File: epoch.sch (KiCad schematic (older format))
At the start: 33 parts, among them J1 USB_OTG, J2 CONN_01X05, P3 CONN_01X10, SW1 SW_Reset, SW2 SW_Up, SW3 SW_Middle, SW4 SW_Down, U1 MIC5219-3.3BM5, U2 ATSAMD21Ennc-AU, U3 DS3231MZ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

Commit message: Increase drill size to 2.1.  Rework daughter board
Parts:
- U6, U7, U8, U9: footprint my-fp-library:MH2mm -> my-fp-library:MH2.1mm; symbol MH2mm -> MH2.1mm
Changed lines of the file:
@@
 $EndComp
 $Comp
-L MH2mm U6
+L MH2.1mm U6
 U 1 1 59C46AF5
 P 10350 2400
 F 0 "U6" H 10450 2400 60  0001 C CNN
 F 1 "MH2mm" H 10350 2700 60  0001 C CNN
-F 2 "my-fp-library:MH2mm" H 10350 2400 60  0001 C CNN
+F 2 "my-fp-library:MH2.1mm" H 10350 2400 60  0001 C CNN
 F 3 "" H 10350 2400 60  0001 C CNN
 	1    10350 2400
@@
 $EndComp
 $Comp
-L MH2mm U7
+L MH2.1mm U7
 U 1 1 59C46D36
 P 10350 2550
 F 0 "U7" H 10450 2550 60  0001 C CNN
 F 1 "MH2mm" H 10350 2850 60  0001 C CNN
-F 2 "my-fp-library:MH2mm" H 10350 2550 60  0001 C CNN
+F 2 "my-fp-library:MH2.1mm" H 10350 2550 60  0001 C CNN
 F 3 "" H 10350 2550 60  0001 C CNN
 	1    10350 2550
@@
 $EndComp
 $Comp
-L MH2mm U8
+L MH2.1mm U8
 U 1 1 59C46DAD
 P 10350 2700
 F 0 "U8" H 10450 2700 60  0001 C CNN
 F 1 "MH2mm" H 10350 3000 60  0001 C CNN
-F 2 "my-fp-library:MH2mm" H 10350 2700 60  0001 C CNN
+F 2 "my-fp-library:MH2.1mm" H 10350 2700 60  0001 C CNN
 F 3 "" H 10350 2700 60  0001 C CNN
 	1    10350 2700
@@
 $EndComp
 $Comp
-L MH2mm U9
+L MH2.1mm U9
 U 1 1 59C46E3F
 P 10350 2850
 F 0 "U9" H 10450 2850 60  0001 C CNN
 F 1 "MH2mm" H 10350 3150 60  0001 C CNN
-F 2 "my-fp-library:MH2mm" H 10350 2850 60  0001 C CNN
+F 2 "my-fp-library:MH2.1mm" H 10350 2850 60  0001 C CNN
 F 3 "" H 10350 2850 60  0001 C CNN
 	1    10350 2850

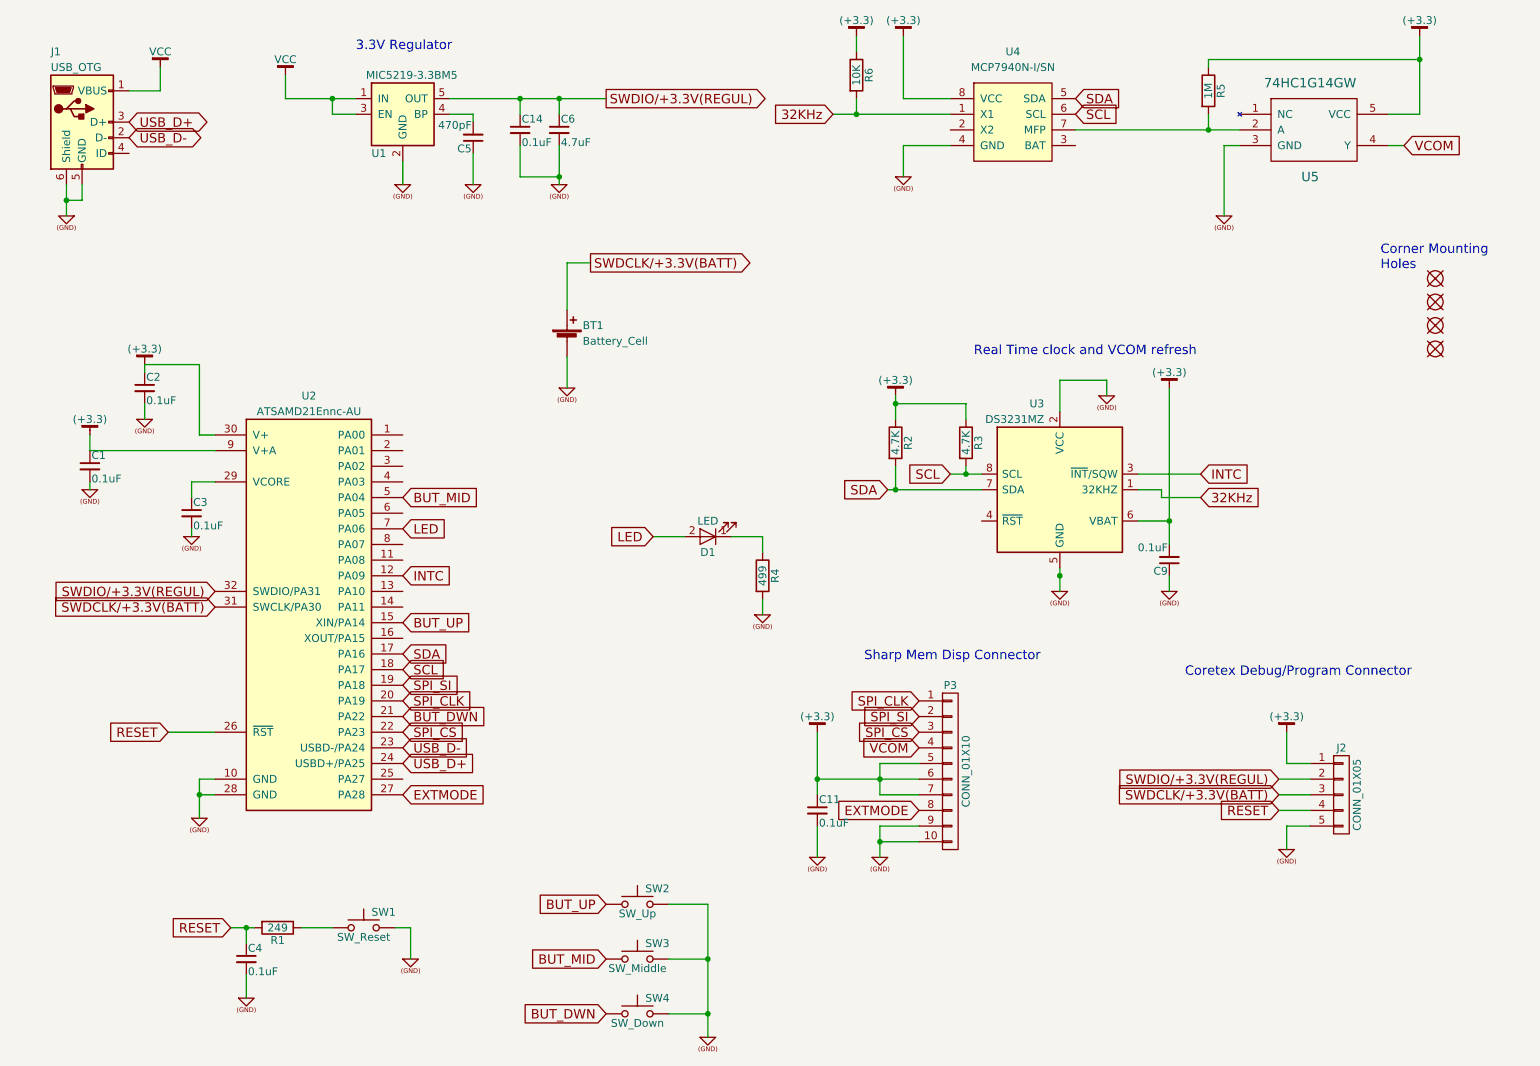
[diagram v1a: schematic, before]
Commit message: update for RTC battery grounding and clock pull-up increased to 1M to reduce power consumption
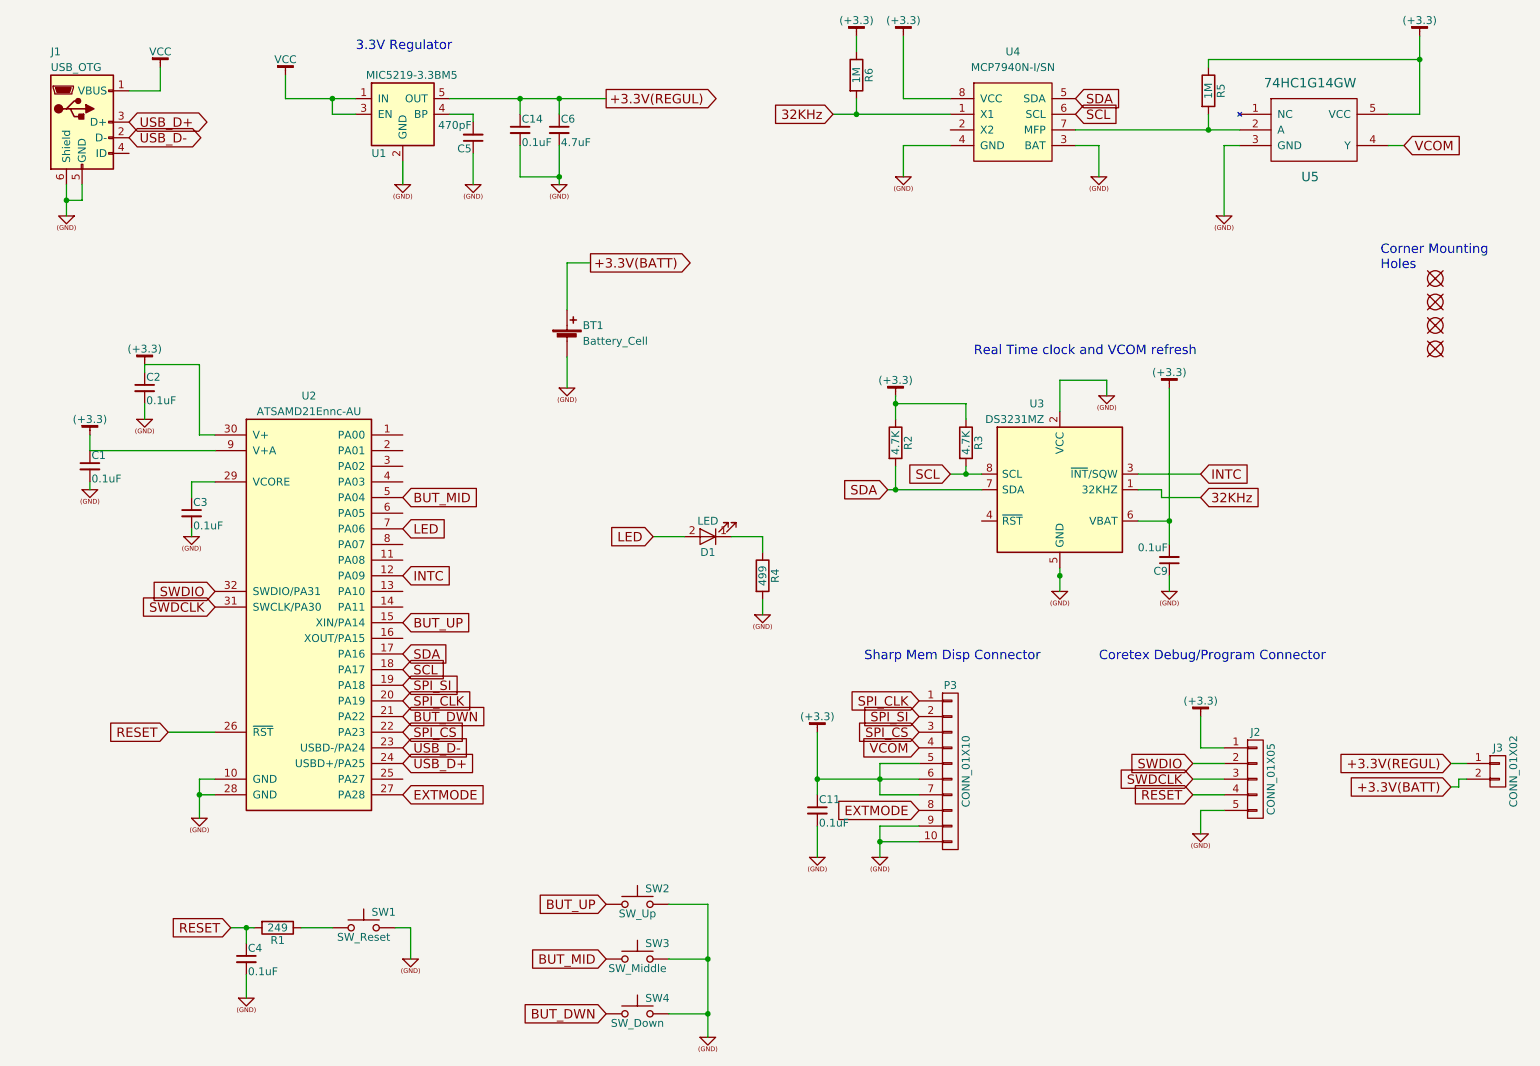
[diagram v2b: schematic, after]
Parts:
- added J3: CONN_01X02, Pin_Headers:Pin_Header_Straight_1x02_Pitch1.27mm, symbol CONN_01X02
- R6: value 10K -> 1M
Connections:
- net (GND): now also U4.3 (BAT)
- net SWDCLK/+3.3V(BATT) renamed SWDCLK
- net SWDCLK: no longer BT1.1 (+)
- net SWDIO/+3.3V(REGUL) renamed +3.3V(REGUL)
- net +3.3V(REGUL): now also J3.1 (P1); no longer J2.2 (P2), U2.32 (SWDIO/PA31)
- new net +3.3V(BATT): BT1.1 (+), J3.2 (P2)
- new net SWDIO: J2.2 (P2), U2.32 (SWDIO/PA31)
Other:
- moved on the sheet: J2
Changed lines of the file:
@@
 	1    0    0    -1
 $EndComp
-Text Notes 8750 4950 0    60   ~ 0
+Text Notes 8200 4850 0    60   ~ 0
 Coretex Debug/Program Connector
 $Comp
@@
 L CONN_01X05 J2
 U 1 1 58FD226D
-P 9750 5700
-F 0 "J2" H 9750 6000 50  0000 C CNN
-F 1 "CONN_01X05" V 9850 5700 50  0000 C CNN
-F 2 "Pin_Headers:Pin_Header_Straight_1x05_Pitch1.27mm" H 9750 5700 50  0001 C CNN
-F 3 "" H 9750 5700 50  0001 C CNN
-	1    9750 5700
+P 9200 5600
+F 0 "J2" H 9200 5900 50  0000 C CNN
+F 1 "CONN_01X05" V 9300 5600 50  0000 C CNN
+F 2 "Pin_Headers:Pin_Header_Straight_1x05_Pitch1.27mm" H 9200 5600 50  0001 C CNN
+F 3 "" H 9200 5600 50  0001 C CNN
+	1    9200 5600
 	1    0    0    -1
 $EndComp
@@
 L (+3.3) #PWR023
 U 1 1 58FD27AF
-P 9400 5300
-F 0 "#PWR023" H 9400 5350 30  0001 C CNN
-F 1 "(+3.3)" H 9400 5400 50  0000 C CNN
-F 2 "" H 9400 5300 60  0000 C CNN
-F 3 "" H 9400 5300 60  0000 C CNN
-	1    9400 5300
-	1    0    0    -1
-$EndComp
-Text GLabel 9350 5600 0    60   Input ~ 0
-SWDIO/+3.3V(REGUL)
-Text GLabel 9350 5700 0    60   Input ~ 0
-SWDCLK/+3.3V(BATT)
-Text GLabel 9350 5800 0    60   Input ~ 0
+P 8850 5200
+F 0 "#PWR023" H 8850 5250 30  0001 C CNN
+F 1 "(+3.3)" H 8850 5300 50  0000 C CNN
+F 2 "" H 8850 5200 60  0000 C CNN
+F 3 "" H 8850 5200 60  0000 C CNN
+	1    8850 5200
+	1    0    0    -1
+$EndComp
+Text GLabel 8800 5500 0    60   Input ~ 0
+SWDIO
+Text GLabel 8800 5600 0    60   Input ~ 0
+SWDCLK
+Text GLabel 8800 5700 0    60   Input ~ 0
 RESET
 $Comp
 L (GND) #PWR024
 U 1 1 58FD2934
-P 9400 6050
-F 0 "#PWR024" H 9400 6050 30  0001 C CNN
-F 1 "(GND)" H 9400 6050 30  0001 C CNN
-F 2 "" H 9400 6050 60  0000 C CNN
-F 3 "" H 9400 6050 60  0000 C CNN
-	1    9400 6050
+P 8850 5950
+F 0 "#PWR024" H 8850 5950 30  0001 C CNN
+F 1 "(GND)" H 8850 5950 30  0001 C CNN
+F 2 "" H 8850 5950 60  0000 C CNN
+F 3 "" H 8850 5950 60  0000 C CNN
+	1    8850 5950
 	1    0    0    -1
 $EndComp
@@
 P 6650 1100
 F 0 "R6" V 6730 1100 50  0000 C CNN
-F 1 "10K" V 6650 1100 50  0000 C CNN
+F 1 "1M" V 6650 1100 50  0000 C CNN
 F 2 "Resistors_SMD:R_0805_HandSoldering" V 6580 1100 50  0001 C CNN
 F 3 "" H 6650 1100 50  0000 C CNN
@@
 	4750 1250 4750 1350
 Wire Wire Line
-	9550 5800 9350 5800
-Wire Wire Line
-	9550 5900 9400 5900
-Wire Wire Line
-	9400 5900 9400 6050
-Wire Wire Line
-	9550 5500 9400 5500
-Wire Wire Line
-	9400 5500 9400 5300
+	9000 5700 8800 5700
+Wire Wire Line
+	9000 5800 8850 5800
+Wire Wire Line
+	8850 5800 8850 5950
+Wire Wire Line
+	9000 5400 8850 5400
+Wire Wire Line
+	8850 5400 8850 5200
 Wire Wire Line
 	4050 1350 4200 1350
@@
 	4800 2300 4950 2300
 Text GLabel 5050 1250 2    60   Output ~ 0
-SWDIO/+3.3V(REGUL)
++3.3V(REGUL)
 Text GLabel 2550 4400 0    60   Input ~ 0
-SWDIO/+3.3V(REGUL)
-Wire Wire Line
-	9350 5600 9550 5600
-Wire Wire Line
-	9350 5700 9550 5700
+SWDIO
+Wire Wire Line
+	8800 5500 9000 5500
+Wire Wire Line
+	8800 5600 9000 5600
 Text GLabel 4950 2300 2    60   Output ~ 0
-SWDCLK/+3.3V(BATT)
++3.3V(BATT)
 Text GLabel 2550 4500 0    60   Input ~ 0
-SWDCLK/+3.3V(BATT)
+SWDCLK
+$Comp
+L CONN_01X02 J3
+U 1 1 5A087ADC
+P 10750 5550
+F 0 "J3" H 10750 5700 50  0000 C CNN
+F 1 "CONN_01X02" V 10850 5550 50  0000 C CNN
+F 2 "Pin_Headers:Pin_Header_Straight_1x02_Pitch1.27mm" H 10750 5550 50  0001 C CNN
+F 3 "" H 10750 5550 50  0001 C CNN
+	1    10750 5550
+	1    0    0    -1
+$EndComp
+Text GLabel 10450 5500 0    60   Input ~ 0
++3.3V(REGUL)
+Text GLabel 10450 5650 0    60   Input ~ 0
++3.3V(BATT)
+Wire Wire Line
+	10550 5500 10450 5500
+Wire Wire Line
+	10550 5600 10500 5600
+Wire Wire Line
+	10500 5600 10500 5650
+Wire Wire Line
+	10500 5650 10450 5650
+$Comp
+L (GND) #PWR?
+U 1 1 5A77AE70
+P 8200 1750
+F 0 "#PWR?" H 8200 1750 30  0001 C CNN
+F 1 "(GND)" H 8200 1750 30  0001 C CNN
+F 2 "" H 8200 1750 60  0000 C CNN
+F 3 "" H 8200 1750 60  0000 C CNN
+	1    8200 1750
+	1    0    0    -1
+$EndComp
+Wire Wire Line
+	8050 1550 8200 1550
+Wire Wire Line
+	8200 1550 8200 1750
 $EndSCHEMATC
